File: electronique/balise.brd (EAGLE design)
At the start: 160 x 100 mm, 46 parts

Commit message: maj elec balise
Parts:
- added LED1, LED13, LED14, LED15, LED16, LED17, LED18, LED19, LED2, LED3: orange, led:LED5MM
- added LED10, LED11, LED12: bleu, led:LED5MM
- added LED4, LED5, LED6: jaune, led:LED5MM
- added LED7, LED8, LED9: vert, led:LED5MM
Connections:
- removed net DEL_CH_1: R10.2, R12.2, R14.2, R16.2, R18.2, R2.2, R20.2, R22.2, R24.2, R6.2, R8.2
- removed net DEL_CH_2: R4.2
- removed net DEL_CTRL_1: R1.2, R11.2, R13.2, R15.2, R17.2, R19.2, R21.2, R23.2, R7.2, R9.2
- removed net DEL_CTRL_2: R3.2
- removed net DEL_CTRL_3: R5.2
- removed net N$28: RPI.11
- removed net N$29: RPI.13
- removed net N$30: RPI.15
- removed net N$31: RPI.29
- removed net N$32: RPI.31
- removed net N$33: RPI.33
- removed net N$34: RPI.35
- removed net N$35: RPI.37
- removed net N$36: RPI.19
- removed net N$37: RPI.21
- removed net N$38: RPI.23
- new net DEL_BLEU_1: LED10.A, R20.2
- new net DEL_BLEU_1_PWM: R19.2, RPI.35
- new net DEL_BLEU_2: LED11.A, R22.2
- new net DEL_BLEU_2_PWM: R21.2, RPI.37
- new net DEL_BLEU_3: LED12.A, R24.2
- new net DEL_BLEU_3_PWM: R23.2, RPI.40
- new net DEL_JAUNE_1: LED4.A, LED5.A, LED6.A, R14.2
- new net DEL_JAUNE_1_PWM: R13.2, RPI.19
- new net DEL_JAUNE_2: R16.2
- new net DEL_JAUNE_2_PWM: R15.2, RPI.21
- new net DEL_JAUNE_3: R18.2
- new net DEL_JAUNE_3_PWM: R17.2, RPI.23
- new net DEL_ORANGE_1: LED1.A, R2.2
- new net DEL_ORANGE_1_PWM: R1.2, RPI.11
- new net DEL_ORANGE_2: LED2.A, R4.2
- new net DEL_ORANGE_2_PWM: R3.2, RPI.13
- new net DEL_ORANGE_3: LED3.A, R6.2
- new net DEL_ORANGE_3_PWM: R5.2, RPI.15
- new net DEL_VERT_1: LED7.A, R8.2
- new net DEL_VERT_1_PWM: R7.2, RPI.29
- new net DEL_VERT_2: LED8.A, R10.2
- new net DEL_VERT_2_PWM: R9.2, RPI.31
- new net DEL_VERT_3: LED9.A, R12.2
- new net DEL_VERT_3_PWM: R11.2, RPI.33
- net GND: now also LED1.K, LED10.K, LED11.K, LED12.K, LED2.K, LED3.K, LED4.K, LED5.K, LED6.K, LED7.K, LED8.K, LED9.K

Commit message: Ajout élec balise
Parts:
- removed LED1, LED13, LED14, LED15, LED16, LED17, LED18, LED19, LED2, LED3: orange, led:LED5MM
- removed LED10, LED11, LED12: bleu, led:LED5MM
- removed LED4, LED5, LED6: jaune, led:LED5MM
- removed LED7, LED8, LED9: vert, led:LED5MM
- removed R10, R12, R2, R4, R6, R8: 0, resistor:R0805
- removed R11, R3, R5, R7, R9: 270, resistor:R0805
- removed T1, T10, T11, T12, T2, T3, T4, T9: (no value), transistor:SOT23-BEC
- added C3: 10µF, resistor:C0805
- added LED100, LED117, LED118, LED119, LED120, LED121, LED122, LED123, LED132, LED149, LED150, LED151, LED152, LED153, LED154, LED155, LED34, LED51, LED52, LED53, LED54, LED55, LED56, LED57: jaune, led:LED5MM
- added LED101, LED110, LED111, LED112, LED113, LED114, LED115, LED116, LED133, LED142, LED143, LED144, LED145, LED146, LED147, LED148, LED35, LED44, LED45, LED46, LED47, LED48, LED49, LED50, LED97: vert, led:LED5MM
- added LED102, LED124, LED125, LED126, LED127, LED128, LED129, LED130, LED134, LED156, LED157, LED158, LED159, LED160, LED161, LED162, LED36, LED58, LED59, LED60, LED61, LED62, LED63, LED64, LED98: bleu, led:LED5MM
- added LED103, LED104, LED105, LED106, LED107, LED108, LED109, LED131, LED135, LED136, LED137, LED138, LED139, LED140, LED141, LED33, LED37, LED38, LED39, LED40, LED41, LED42, LED43, LED99: orange, led:LED5MM
- added R37: 1k, resistor:R0805
- added R38: 470, resistor:R0805
- added R39, R40, R41, R42, R43, R44, R45, R46, R51, R52, R53, R54, R55, R56, R57, R58: 0, resistor:R0805
- added R47, R48, R49, R50, R59, R60, R61, R62: 270, resistor:R0805
- added T13, T14, T15, T16, T17, T18, T19, T20: (no value), transistor:SOT23-BEC
- added U$1: PUSH-BUTTON, push-button:PUSH-BUTTON
- R1: value 270 -> 1k
- R13, R15, R17, R19: value 270 -> 0
- R22, R24: value 0 -> 270
- moved R21 325.2 mm to (26.6, 121.6), turned to 90 degrees
- moved R22 324.7 mm to (35.2, 120.0), turned to 90 degrees
- moved R24 322.8 mm to (11.0, 115.6), turned to 90 degrees
- moved R16 319.0 mm to (33.0, 116.8), turned to 90 degrees
- moved R23 317.0 mm to (18.2, 120.0), turned to 90 degrees
- moved R20 312.5 mm to (8.80, 112.4), turned to 90 degrees
- moved R17 309.3 mm to (13.8, 116.4), turned to 90 degrees
- moved R18 308.5 mm to (16.0, 116.8), turned to 90 degrees
- moved R13 307.0 mm to (22.2, 118.4), turned to 90 degrees
- moved R14 305.6 mm to (24.4, 118.4), turned to 90 degrees
- moved R15 304.3 mm to (30.8, 116.8), turned to 90 degrees
- moved R19 296.8 mm to (7.40, 109.2), turned to 180 degrees
- moved T7 293.7 mm to (19.2, 116.4), turned to 270 degrees
- moved T8 286.1 mm to (12.8, 112.0), turned to 270 degrees
- moved T6 283.6 mm to (36.2, 116.4), turned to 270 degrees
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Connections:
- removed net +3V3: DC2.3, T1.C, T10.C, T11.C, T12.C, T2.C, T3.C, T4.C, T5.C, T6.C, T7.C, T8.C, T9.C
- removed net N$10: R7.1, T4.B
- removed net N$16: R13.1, T7.B
- removed net N$17: R14.1, T7.E
- removed net N$19: R16.1, T8.E
- removed net N$22: R19.1, T10.B
- removed net N$24: R21.1, T11.B
- removed net N$25: R22.1, T11.E
- removed net N$26: R23.1, T12.B
- removed net N$27: R24.1, T12.E
- removed net N$3: R1.1, T1.B
- removed net N$5: R2.1, T1.E
- removed net N$7: R4.1, T2.E
- new net 3V3@1: R1.1, RPI.1
- new net DEL_POWER: DC2.3, T13.C, T14.C, T15.C, T16.C, T17.C, T18.C, T19.C, T20.C, T5.C, T6.C, T7.C, T8.C
- new net N$40: LED97.A, R37.2
- new net N$41: R38.1, RPI.38
- new net N$42: LED98.A, R38.2
- new net N$43: LED103.K, LED104.K, LED105.K, LED99.K, R39.1
- new net N$44: LED106.K, LED107.K, LED108.K, LED109.K, R40.1
- new net N$45: LED101.K, LED110.K, LED111.K, LED112.K, R41.1
- new net N$46: LED113.K, LED114.K, LED115.K, LED116.K, R42.1
- new net N$47: LED100.K, LED117.K, LED118.K, LED119.K, R43.1
- new net N$48: LED120.K, LED121.K, LED122.K, LED123.K, R44.1
- new net N$49: LED102.K, LED124.K, LED125.K, LED126.K, R45.1
- new net N$50: LED127.K, LED128.K, LED129.K, LED130.K, R46.1
- new net N$51: R47.1, T13.B
- new net N$52: R48.1, T14.B
- new net N$53: R49.1, T15.B
- new net N$54: R50.1, T16.B
- new net N$55: LED131.K, LED135.K, LED136.K, LED137.K, R51.1
- new net N$56: LED138.K, LED139.K, LED140.K, LED141.K, R52.1
- new net N$57: LED133.K, LED142.K, LED143.K, LED144.K, R53.1
- new net N$58: LED145.K, LED146.K, LED147.K, LED148.K, R54.1
- new net N$59: LED132.K, LED149.K, LED150.K, LED151.K, R55.1
- new net N$60: LED152.K, LED153.K, LED154.K, LED155.K, R56.1
- new net N$61: LED134.K, LED156.K, LED157.K, LED158.K, R57.1
- new net N$62: LED159.K, LED160.K, LED161.K, LED162.K, R58.1
- new net N$63: R59.1, T17.B
- new net N$64: R60.1, T18.B
- new net N$65: R61.1, T19.B
- new net N$66: R62.1, T20.B
- new net POWEROFF: C3.2, R1.2, RPI.36, U$1.1, U$1.2
- net +5V: now also R37.1
- net DEL_BLEU_1: now also LED134.A, LED156.A, LED157.A, LED158.A, LED159.A, LED160.A, LED161.A, LED162.A, T20.E; no longer LED10.A, R20.2
- net DEL_BLEU_1_PWM: now also R62.2; no longer R19.2
- net DEL_BLEU_2: now also LED36.A, LED58.A, LED59.A, LED60.A, LED61.A, LED62.A, LED63.A, LED64.A, T8.E; no longer LED11.A, R22.2
- net DEL_BLEU_2_PWM: now also R24.2; no longer R21.2
- net DEL_BLEU_3: now also LED102.A, LED124.A, LED125.A, LED126.A, LED127.A, LED128.A, LED129.A, LED130.A, T16.E; no longer LED12.A, R24.2
- net DEL_BLEU_3_PWM: now also R50.2; no longer R23.2
- net DEL_JAUNE_1: now also LED132.A, LED149.A, LED150.A, LED151.A, LED152.A, LED153.A, LED154.A, LED155.A, T19.E; no longer LED4.A, LED5.A, LED6.A, R14.2
- net DEL_JAUNE_1_PWM: now also R61.2; no longer R13.2
- net DEL_JAUNE_2: now also LED34.A, LED51.A, LED52.A, LED53.A, LED54.A, LED55.A, LED56.A, LED57.A, T7.E; no longer R16.2
- net DEL_JAUNE_2_PWM: now also R23.2; no longer R15.2
- net DEL_JAUNE_3: now also LED100.A, LED117.A, LED118.A, LED119.A, LED120.A, LED121.A, LED122.A, LED123.A, T15.E; no longer R18.2
- net DEL_JAUNE_3_PWM: now also R49.2; no longer R17.2
- net DEL_ORANGE_1: now also LED131.A, LED135.A, LED136.A, LED137.A, LED138.A, LED139.A, LED140.A, LED141.A, T17.E; no longer LED1.A, R2.2
- net DEL_ORANGE_1_PWM: now also R59.2; no longer R1.2
- net DEL_ORANGE_2: now also LED33.A, LED37.A, LED38.A, LED39.A, LED40.A, LED41.A, LED42.A, LED43.A, T5.E; no longer LED2.A, R4.2
- net DEL_ORANGE_2_PWM: now also R21.2; no longer R3.2
- net DEL_ORANGE_3: now also LED103.A, LED104.A, LED105.A, LED106.A, LED107.A, LED108.A, LED109.A, LED99.A, T13.E; no longer LED3.A, R6.2
- net DEL_ORANGE_3_PWM: now also R47.2; no longer R5.2
- net DEL_VERT_1: now also LED133.A, LED142.A, LED143.A, LED144.A, LED145.A, LED146.A, LED147.A, LED148.A, T18.E; no longer LED7.A, R8.2
- net DEL_VERT_1_PWM: now also R60.2; no longer R7.2
- net DEL_VERT_2: now also LED35.A, LED44.A, LED45.A, LED46.A, LED47.A, LED48.A, LED49.A, LED50.A, T6.E; no longer LED8.A, R10.2
- net DEL_VERT_2_PWM: now also R22.2; no longer R9.2
- net DEL_VERT_3: now also LED101.A, LED110.A, LED111.A, LED112.A, LED113.A, LED114.A, LED115.A, LED116.A, T14.E; no longer LED9.A, R12.2
- net DEL_VERT_3_PWM: now also R48.2; no longer R11.2
- net GND: now also C3.1, LED97.K, LED98.K, R13.2, R14.2, R15.2, R16.2, R17.2, R18.2, R19.2, R20.2, R39.2, R40.2, R41.2, R42.2, R43.2, R44.2, R45.2, R46.2, R51.2, R52.2, R53.2, R54.2, R55.2, R56.2, R57.2, R58.2, U$1.3, U$1.4; no longer LED1.K, LED10.K, LED11.K, LED12.K, LED2.K, LED3.K, LED4.K, LED5.K, LED6.K, LED7.K, LED8.K, LED9.K
- net N$11: now also LED47.K, LED48.K, LED49.K, LED50.K, R16.1; no longer R8.1, T4.E
- net N$12: now also LED34.K, LED51.K, LED52.K, LED53.K, R17.1; no longer R9.1, T5.B
- net N$13: now also LED54.K, LED55.K, LED56.K, LED57.K, R18.1; no longer R10.1, T5.E
- net N$14: now also LED36.K, LED58.K, LED59.K, LED60.K, R19.1; no longer R11.1, T6.B
- net N$15: now also LED61.K, LED62.K, LED63.K, LED64.K, R20.1; no longer R12.1, T6.E
- net N$18: now also R21.1, T5.B; no longer R15.1, T8.B
- net N$20: now also R22.1, T6.B; no longer R17.1, T9.B
- net N$21: now also R23.1, T7.B; no longer R18.1, T9.E
- net N$23: now also R24.1, T8.B; no longer R20.1, T10.E
- net N$6: now also LED33.K, LED37.K, LED38.K, LED39.K, R13.1; no longer R3.1, T2.B
- net N$8: now also LED40.K, LED41.K, LED42.K, LED43.K, R14.1; no longer R5.1, T3.B
- net N$9: now also LED35.K, LED44.K, LED45.K, LED46.K, R15.1; no longer R6.1, T3.E
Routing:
- net DEL_BLEU_3: track 0.00 -> 130.8 mm, vias 0 -> 2
- net DEL_BLEU_2: track 0.00 -> 130.8 mm, vias 0 -> 2
- net DEL_BLEU_1: track 0.00 -> 130.8 mm, vias 0 -> 2
- net DEL_POWER: track 0.00 -> 124.5 mm, vias 0 -> 12
- net DEL_JAUNE_3: track 0.00 -> 107.7 mm
- net DEL_JAUNE_2: track 0.00 -> 107.7 mm
- net DEL_JAUNE_1: track 0.00 -> 107.7 mm
- net GND: track 0.00 -> 106.2 mm
- net DEL_ORANGE_2: track 0.00 -> 103.6 mm, vias 0 -> 1
- net DEL_ORANGE_1: track 0.00 -> 103.6 mm, vias 0 -> 1
- net DEL_ORANGE_3: track 0.00 -> 103.6 mm, vias 0 -> 1
- net DEL_VERT_3: track 0.00 -> 103.3 mm, vias 0 -> 2
- net DEL_VERT_2: track 0.00 -> 103.3 mm, vias 0 -> 2
- net DEL_VERT_1: track 0.00 -> 103.3 mm, vias 0 -> 2
- net N$50: track 0.00 -> 92.6 mm
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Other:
- board size 160 x 100 mm -> 63 x 191 mm
- board text added: "B"
- board text added: "J"
- board text added: "O"
- board text added: "V"

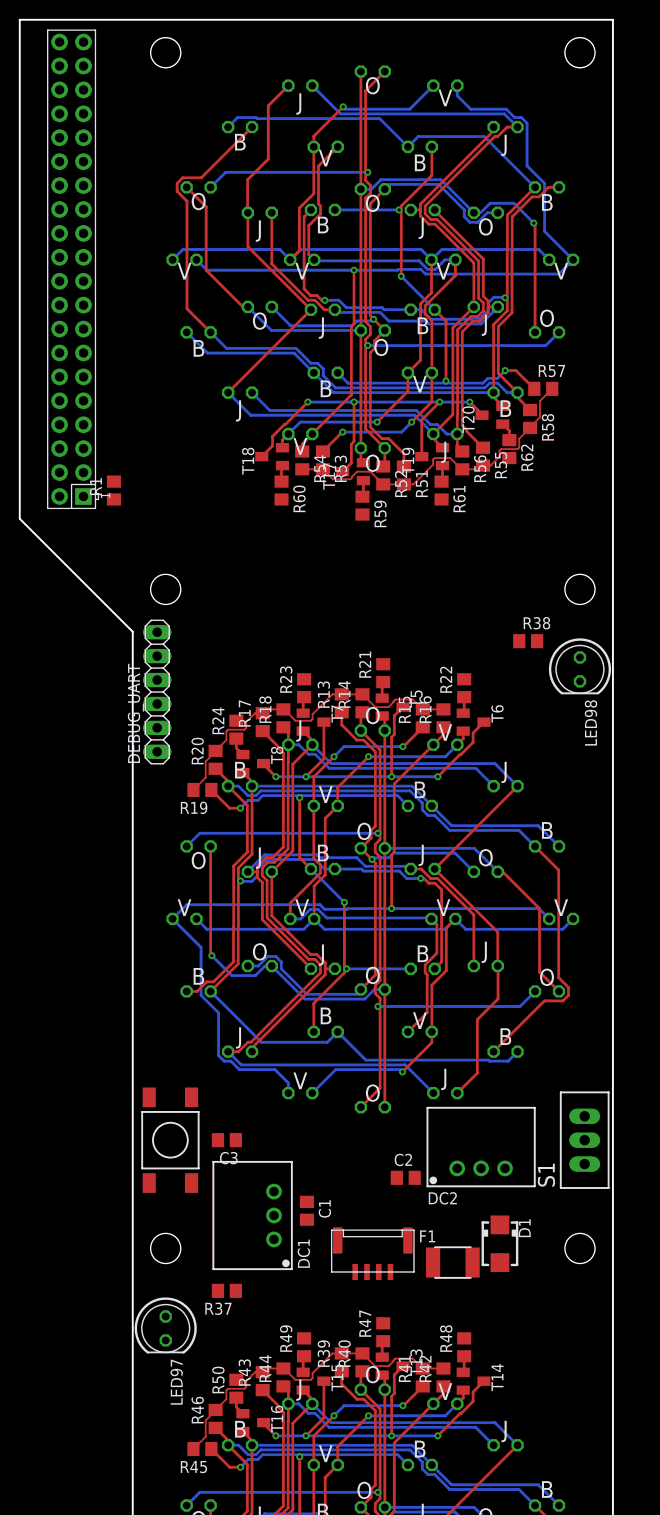
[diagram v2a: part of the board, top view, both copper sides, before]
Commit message: Elec balise routée !
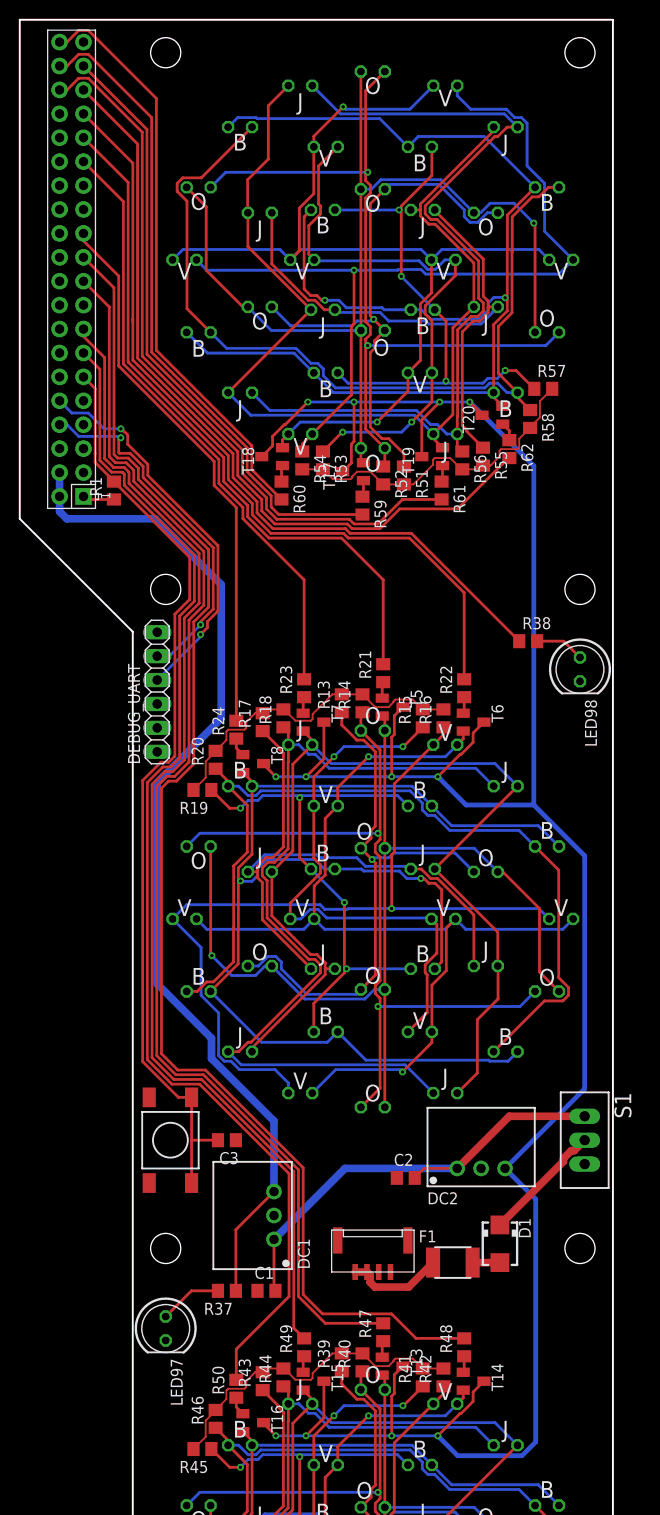
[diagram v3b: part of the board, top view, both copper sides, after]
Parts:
- moved C1 9.53 mm to (14.2, 56.0), turned to 0 degrees
- turned S1 to 270 degrees
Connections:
- removed net N$41: R38.1, RPI.38
- new net STATUS_LED: R38.1, RPI.35
- net DEL_BLEU_1_PWM: now also RPI.36; no longer RPI.35
- net DEL_BLEU_2_PWM: now also RPI.23; no longer RPI.37
- net DEL_BLEU_3_PWM: now also RPI.13; no longer RPI.40
- net DEL_JAUNE_1_PWM: now also RPI.37; no longer RPI.19
- net DEL_JAUNE_2_PWM: now also RPI.29; no longer RPI.21
- net DEL_JAUNE_3_PWM: now also RPI.15; no longer RPI.23
- net DEL_ORANGE_1_PWM: now also RPI.38; no longer RPI.11
- net DEL_ORANGE_2_PWM: now also RPI.31; no longer RPI.13
- net DEL_ORANGE_3_PWM: now also RPI.19; no longer RPI.15
- net DEL_VERT_1_PWM: now also RPI.40; no longer RPI.29
- net DEL_VERT_2_PWM: now also RPI.33; no longer RPI.31
- net DEL_VERT_3_PWM: now also RPI.21; no longer RPI.33
- net POWEROFF: now also RPI.11; no longer RPI.36
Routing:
- net DEL_VERT_3_PWM: track 0.00 -> 145.9 mm
- net DEL_POWER: track 124.5 -> 268.2 mm
- net DEL_ORANGE_3_PWM: track 0.00 -> 134.5 mm
- net DEL_BLEU_3_PWM: track 0.00 -> 127.4 mm
- net DEL_JAUNE_3_PWM: track 0.00 -> 123.9 mm
- net +5V: track 0.00 -> 109.2 mm
- net POWEROFF: track 0.00 -> 98.6 mm
- net DEL_BLEU_1_PWM: track 0.00 -> 87.3 mm
- net STATUS_LED: track 0.00 -> 86.0 mm
- net DEL_VERT_2_PWM: track 0.00 -> 85.1 mm
- net DEL_JAUNE_1_PWM: track 0.00 -> 75.4 mm
- net DEL_ORANGE_2_PWM: track 0.00 -> 73.6 mm
- net DEL_ORANGE_1_PWM: track 0.00 -> 69.7 mm
- net DEL_JAUNE_2_PWM: track 0.00 -> 64.7 mm
- net DEL_VERT_1_PWM: track 0.00 -> 61.9 mm
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
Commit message: Elec version finale + Ajout fichiers gerber
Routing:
- net GND: vias 0 -> 7
- added copper zone on layer 1, net GND
- added copper zone on layer 16, net GND
